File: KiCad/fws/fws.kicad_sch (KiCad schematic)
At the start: 1 part, among them U1 RP2040

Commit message: Updated schematic.
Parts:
- added U2: MIC5205-3.3YM5, Package_TO_SOT_SMD:SOT-23-5, symbol Regulator_Linear:MIC5205-3.3YM5
- added U3: W25Q128JVS, Package_SO:SOIC-8_5.23x5.23mm_P1.27mm, symbol Memory_Flash:W25Q128JVS
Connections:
- new net +3.3V: U2.5 (OUT)
- new net GND: U2.2 (GND)
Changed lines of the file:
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@@
 (kicad_sch (version 20230121) (generator eeschema)
   (paper "A4")
+  (wire (pts (xy 60.96 27.94) (xy 73.66 27.94))
+    (stroke (width 0) (type default))
+  )
+  (wire (pts (xy 53.34 38.1) (xy 53.34 40.64))
+    (stroke (width 0) (type default))
+  )
+  (wire (pts (xy 73.66 27.94) (xy 73.66 26.67))
+    (stroke (width 0) (type default))
+  )
   (symbol (lib_id "MCU_RaspberryPi:RP2040") (at 116.84 96.52 0) (unit 1)
     (in_bom yes) (on_board yes) (dnp no) (fields_autoplaced)
@@
         )
       )
+    )
+  )
+  (symbol (lib_id "Regulator_Linear:MIC5205-3.3YM5") (at 53.34 30.48 0) (unit 1)
+    (in_bom yes) (on_board yes) (dnp no) (fields_autoplaced)
+    (property "Reference" "U2" (at 53.34 21.59 0)
+      (effects (font (size 1.27 1.27)))
+    )
+    (property "Value" "MIC5205-3.3YM5" (at 53.34 24.13 0)
+      (effects (font (size 1.27 1.27)))
+    )
+    (property "Footprint" "Package_TO_SOT_SMD:SOT-23-5" (at 53.34 22.225 0)
+      (effects (font (size 1.27 1.27)) hide)
+    )
+    (property "Datasheet" "http://ww1.microchip.com/downloads/en/DeviceDoc/20005785A.pdf" (at 53.34 30.48 0)
+      (effects (font (size 1.27 1.27)) hide)
+    )
+    (pin "1")
+    (pin "2")
+    (pin "3")
+    (pin "4")
+    (pin "5")
+    (instances
+      (project "fws"
+        (path "/1464a0f5-893a-45f7-94f1-a97986ba6c99"
+          (reference "U2") (unit 1)
+        )
+      )
+    )
+  )
+  (symbol (lib_id "power:+3.3V") (at 73.66 26.67 0) (unit 1)
+    (in_bom yes) (on_board yes) (dnp no) (fields_autoplaced)
+    (property "Reference" "#PWR01" (at 73.66 30.48 0)
+      (effects (font (size 1.27 1.27)) hide)
+    )
+    (property "Value" "+3.3V" (at 73.66 21.59 0)
+      (effects (font (size 1.27 1.27)))
+    )
+    (property "Footprint" "" (at 73.66 26.67 0)
+      (effects (font (size 1.27 1.27)) hide)
+    )
+    (property "Datasheet" "" (at 73.66 26.67 0)
+      (effects (font (size 1.27 1.27)) hide)
+    )
+    (pin "1")
+    (instances
+      (project "fws"
+        (path "/1464a0f5-893a-45f7-94f1-a97986ba6c99"
+          (reference "#PWR01") (unit 1)
+        )
+      )
+    )
+  )
+  (symbol (lib_id "power:GND") (at 53.34 40.64 0) (unit 1)
+    (in_bom yes) (on_board yes) (dnp no) (fields_autoplaced)
+    (property "Reference" "#PWR02" (at 53.34 46.99 0)
+      (effects (font (size 1.27 1.27)) hide)
+    )
+    (property "Value" "GND" (at 53.34 45.72 0)
+      (effects (font (size 1.27 1.27)))
+    )
+    (property "Footprint" "" (at 53.34 40.64 0)
+      (effects (font (size 1.27 1.27)) hide)
+    )
+    (property "Datasheet" "" (at 53.34 40.64 0)
+      (effects (font (size 1.27 1.27)) hide)
+    )
+    (pin "1")
+    (instances
+      (project "fws"
+        (path "/1464a0f5-893a-45f7-94f1-a97986ba6c99"
+          (reference "#PWR02") (unit 1)
+        )
+      )
+    )
+  )
+  (symbol (lib_id "Memory_Flash:W25Q128JVS") (at 204.47 44.45 0) (unit 1)
+    (in_bom yes) (on_board yes) (dnp no) (fields_autoplaced)
+    (property "Reference" "U3" (at 213.36 43.18 0)
+      (effects (font (size 1.27 1.27)) (justify left))
+    )
+    (property "Value" "W25Q128JVS" (at 213.36 45.72 0)
+      (effects (font (size 1.27 1.27)) (justify left))
+    )
+    (property "Footprint" "Package_SO:SOIC-8_5.23x5.23mm_P1.27mm" (at 204.47 44.45 0)
+      (effects (font (size 1.27 1.27)) hide)
+    )
+    (property "Datasheet" "http://www.winbond.com/resource-files/w25q128jv_dtr%20revc%2003272018%20plus.pdf" (at 204.47 44.45 0)
+      (effects (font (size 1.27 1.27)) hide)
+    )
+    (pin "1")
+    (pin "2")
+    (pin "3")
+    (pin "4")
+    (pin "5")
+    (pin "6")
+    (pin "7")
+    (pin "8")
+    (instances
+      (project "fws"
+        (path "/1464a0f5-893a-45f7-94f1-a97986ba6c99"
+          (reference "U3") (unit 1)
+        )
+      )

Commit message: Updated schematics.
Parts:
- added J1, J2: Conn_01x03_Socket, symbol Connector:Conn_01x03_Socket
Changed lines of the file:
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@@
+    )
+  )
+  (symbol (lib_id "Connector:Conn_01x03_Socket") (at 213.36 105.41 0) (unit 1)
+    (in_bom yes) (on_board yes) (dnp no) (fields_autoplaced)
+    (property "Reference" "J1" (at 214.63 104.14 0)
+      (effects (font (size 1.27 1.27)) (justify left))
+    )
+    (property "Value" "Conn_01x03_Socket" (at 214.63 106.68 0)
+      (effects (font (size 1.27 1.27)) (justify left))
+    )
+    (property "Footprint" "" (at 213.36 105.41 0)
+      (effects (font (size 1.27 1.27)) hide)
+    )
+    (property "Datasheet" "~" (at 213.36 105.41 0)
+      (effects (font (size 1.27 1.27)) hide)
+    )
+    (pin "1")
+    (pin "2")
+    (pin "3")
+    (instances
+      (project "fws"
+        (path "/1464a0f5-893a-45f7-94f1-a97986ba6c99"
+          (reference "J1") (unit 1)
+        )
+      )
     )
   )
@@
         )
       )
+    )
+  )
+  (symbol (lib_id "Connector:Conn_01x03_Socket") (at 214.63 121.92 0) (unit 1)
+    (in_bom yes) (on_board yes) (dnp no) (fields_autoplaced)
+    (property "Reference" "J2" (at 215.9 120.65 0)
+      (effects (font (size 1.27 1.27)) (justify left))
+    )
+    (property "Value" "Conn_01x03_Socket" (at 215.9 123.19 0)
+      (effects (font (size 1.27 1.27)) (justify left))
+    )
+    (property "Footprint" "" (at 214.63 121.92 0)
+      (effects (font (size 1.27 1.27)) hide)
+    )
+    (property "Datasheet" "~" (at 214.63 121.92 0)
+      (effects (font (size 1.27 1.27)) hide)
+    )
+    (pin "1")
+    (pin "2")
+    (pin "3")
+    (instances
+      (project "fws"
+        (path "/1464a0f5-893a-45f7-94f1-a97986ba6c99"
+          (reference "J2") (unit 1)
+        )
+      )

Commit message: Various kicad project updates.
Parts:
- removed J1, J2: Conn_01x03_Socket, symbol Connector:Conn_01x03_Socket
- removed U1: RP2040, Package_DFN_QFN:QFN-56-1EP_7x7mm_P0.4mm_EP3.2x3.2mm, symbol MCU_RaspberryPi:RP2040
- removed U2: MIC5205-3.3YM5, Package_TO_SOT_SMD:SOT-23-5, symbol Regulator_Linear:MIC5205-3.3YM5
- removed U3: W25Q128JVS, Package_SO:SOIC-8_5.23x5.23mm_P1.27mm, symbol Memory_Flash:W25Q128JVS
- added J1, J2: SM03B-SRSS-TB_LF__SN_, fws:SM03B-SRSS-TB_LF__SN_, symbol FWS:SM03B-SRSS-TB_LF__SN_
- added U1: MIC5205-3.3YM5, Package_TO_SOT_SMD:SOT-23-5, symbol FWS:MIC5205-3.3YM5
- added U2: RP2040, Package_DFN_QFN:QFN-56-1EP_7x7mm_P0.4mm_EP3.2x3.2mm, symbol FWS:RP2040
- added U3: W25Q128JVS, Package_SO:SOIC-8_5.23x5.23mm_P1.27mm, symbol FWS:W25Q128JVS
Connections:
- new net: U2.1 (IOVDD), U2.10 (IOVDD), U2.22 (IOVDD), U2.33 (IOVDD), U2.42 (IOVDD), U2.49 (IOVDD)
- new net: U2.23 (DVDD), U2.50 (DVDD)
- new net: J2.S1 (SHIELD), J2.S2 (SHIELD)
- new net: J1.S1 (SHIELD), J1.S2 (SHIELD)

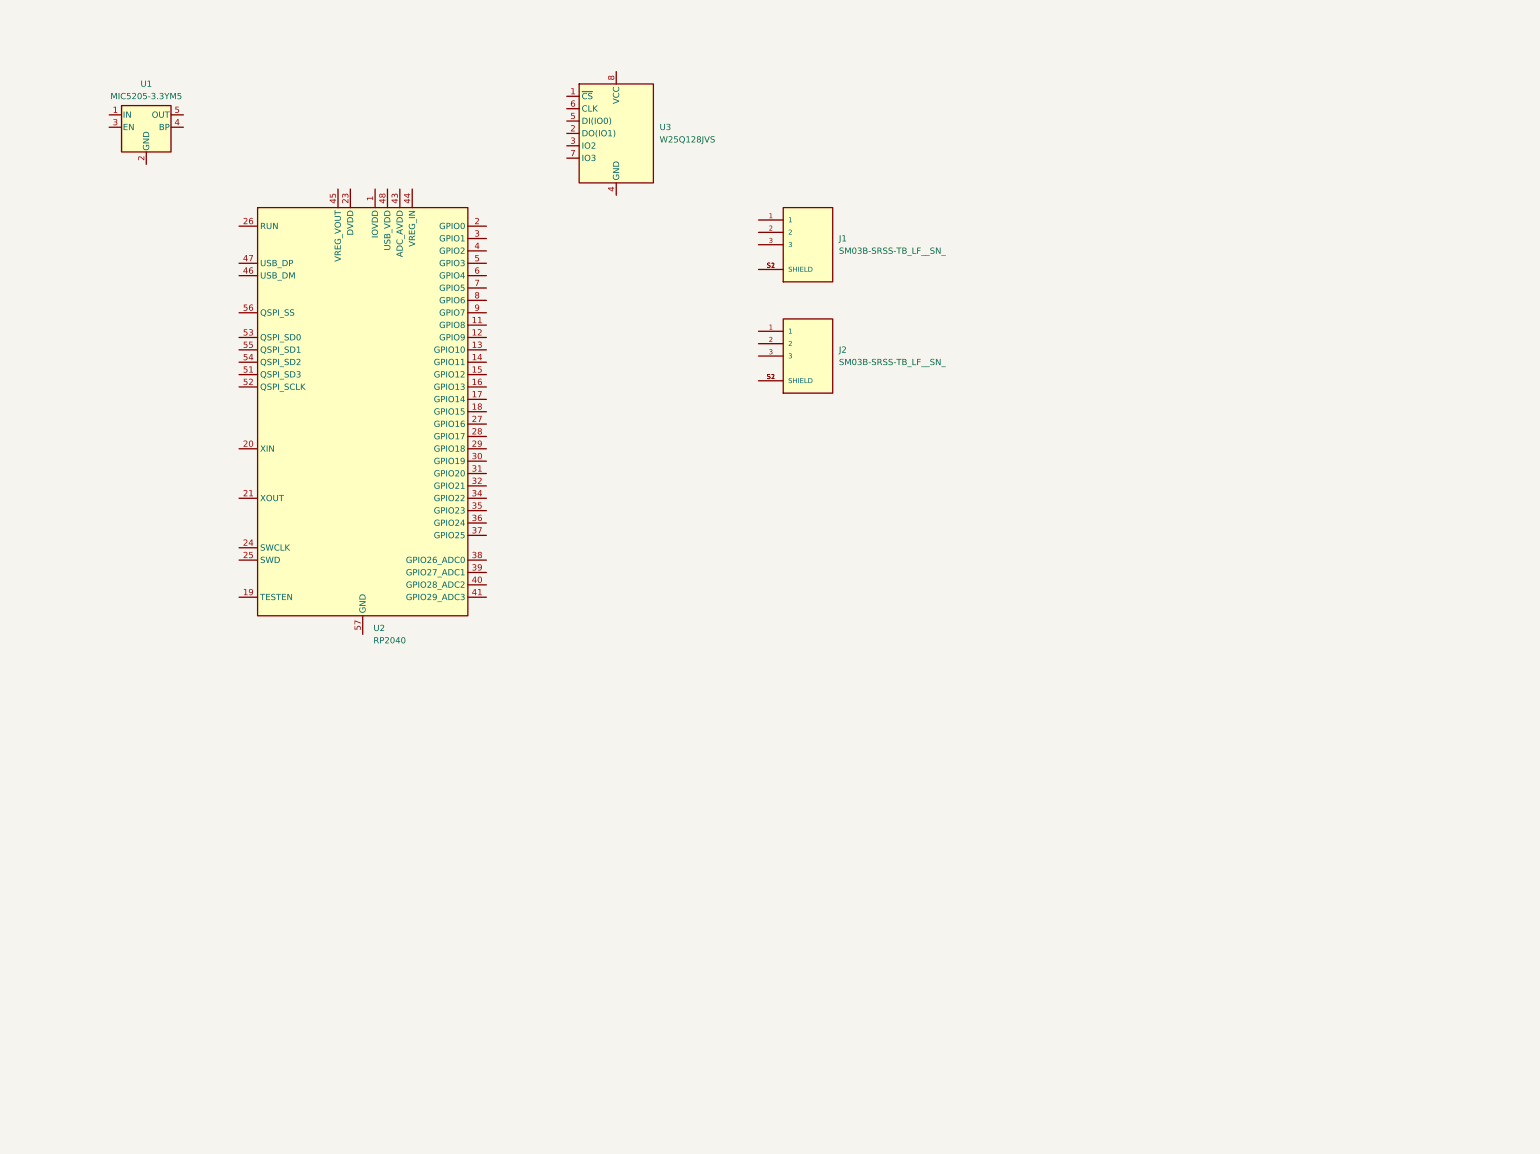
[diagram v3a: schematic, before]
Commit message: Added power and usbc.
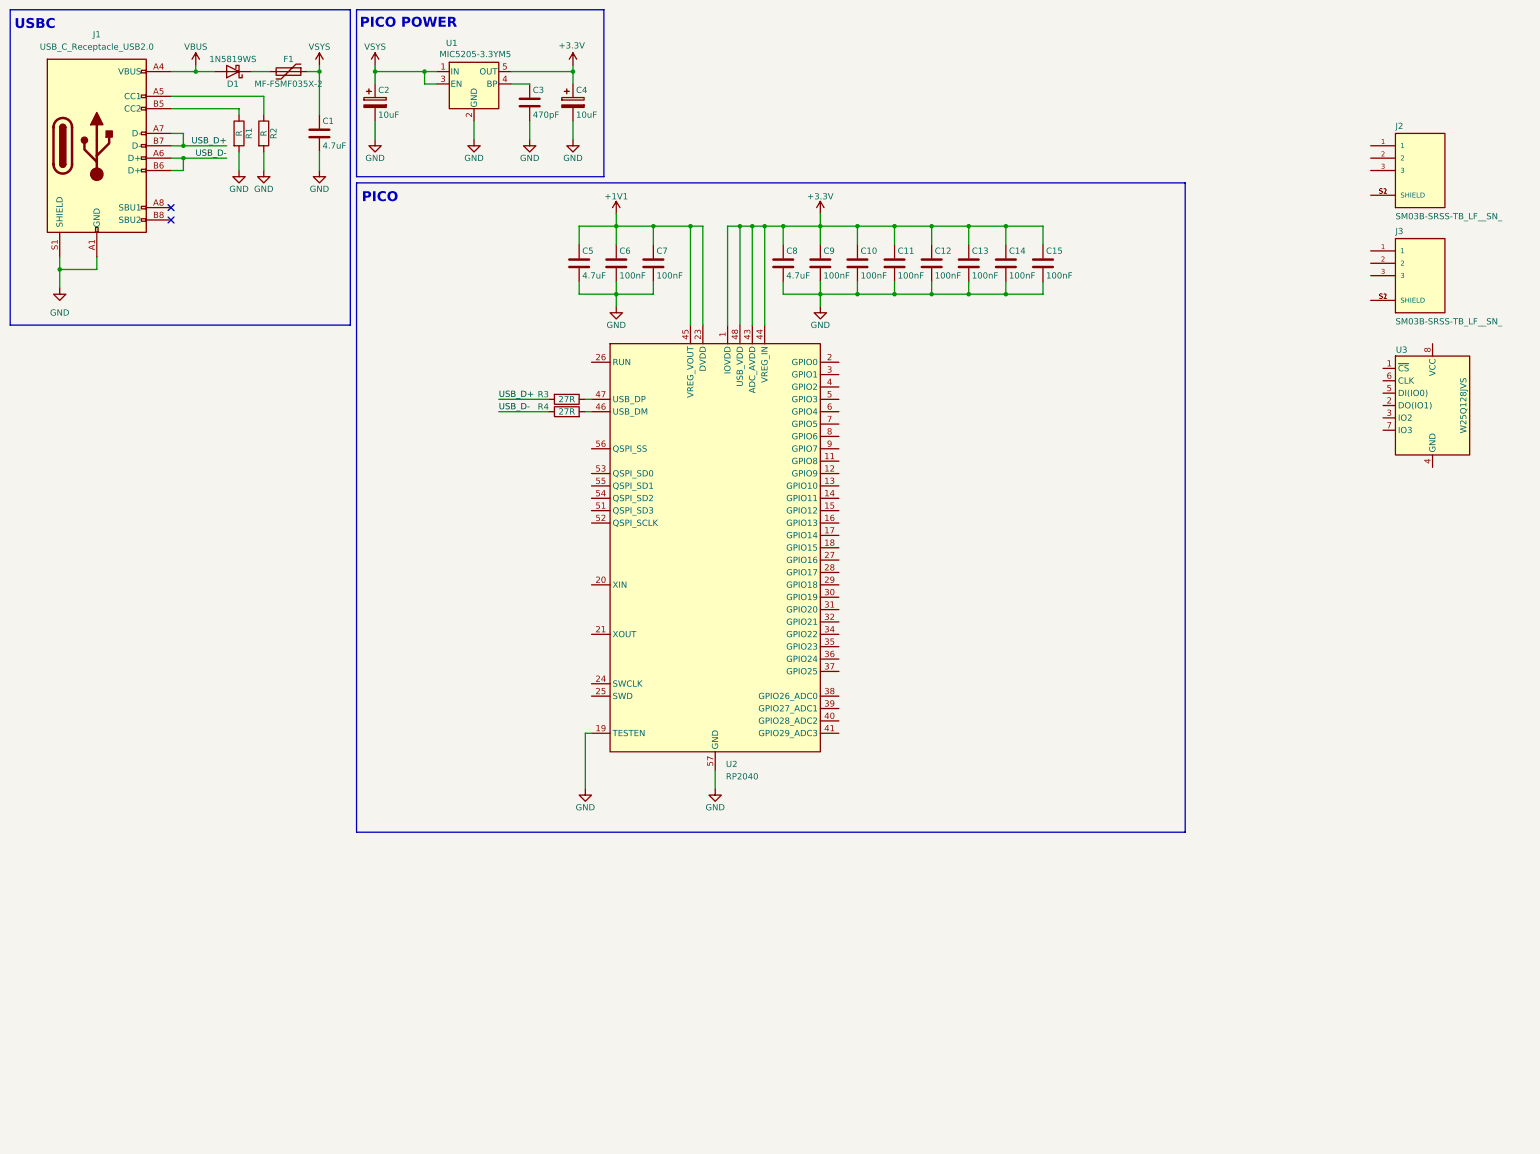
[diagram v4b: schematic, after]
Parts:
- removed J1: SM03B-SRSS-TB_LF__SN_, fws:SM03B-SRSS-TB_LF__SN_, symbol FWS:SM03B-SRSS-TB_LF__SN_
- added C1, C5, C8: 4.7uF, symbol FWS:C
- added C10, C11, C12, C13, C14, C15, C6, C7, C9: 100nF, symbol FWS:C
- added C2, C4: 10uF, symbol FWS:C_Polarized
- added C3: 470pF, symbol FWS:C
- added D1: 1N5819WS, Diode_SMD:D_SOD-323, symbol FWS:1N5819WS
- added F1: MF-FSMF035X-2, symbol FWS:Polyfuse
- added J1: USB_C_Receptacle_USB2.0, symbol FWS:USB_C_Receptacle_USB2.0
- added J3: SM03B-SRSS-TB_LF__SN_, fws:SM03B-SRSS-TB_LF__SN_, symbol FWS:SM03B-SRSS-TB_LF__SN_
- added R1, R2: R, symbol FWS:R
- added R3, R4: 27R, symbol FWS:R
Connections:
- net +3.3V: now reaches U2.1 (IOVDD), U2.10 (IOVDD), U2.22 (IOVDD), U2.33 (IOVDD), U2.42 (IOVDD), U2.49 (IOVDD)
- net +3.3V: now also U1.5 (OUT), U2.43 (ADC_AVDD), U2.44 (VREG_IN), U2.48 (USB_VDD), C10.1, C11.1, C12.1, C13.1, C14.1, C15.1, C4.1, C8.1, C9.1
- net GND: now reaches U2.19 (TESTEN)
- net GND: now also U1.2 (GND), U2.57 (GND), C1.2, C10.2, C11.2, C12.2, C13.2, C14.2, C15.2, C2.2, C3.2, C4.2, C5.2, C6.2, C7.2, C8.2, C9.2, J1.A1 (GND), J1.A12 (GND), J1.B1 (GND), J1.B12 (GND), J1.S1 (SHIELD), R1.2, R2.2
- net +1V1: now reaches U2.23 (DVDD), U2.50 (DVDD)
- net +1V1: now also U2.45 (VREG_VOUT), C5.1, C6.1, C7.1
- net at U2.46 (USB_DM): now also R4.2
- net at U2.47 (USB_DP): now also R3.1
- net VSYS: now reaches U1.1 (IN)
- net VSYS: now also U1.3 (EN), C1.1, C2.1, F1.1
- net at U1.4 (BP): now also C3.1
- new net: J1.A5 (CC1), R2.1
- new net: J1.B5 (CC2), R1.1
- new net: J3.S1 (SHIELD), J3.S2 (SHIELD)
- new net: D1.1 (K), F1.2
- new net USB_D+: J1.A7 (D-), J1.B7 (D-), R3.2
- new net USB_D-: J1.A6 (D+), J1.B6 (D+), R4.1
- new net VBUS: D1.2 (A), J1.A4 (VBUS), J1.A9 (VBUS), J1.B4 (VBUS), J1.B9 (VBUS)
- no-connect marks 0 -> 2
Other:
- note added: "PICO"
- note added: "PICO POWER"
- note added: "USBC"
- moved on the sheet: U2

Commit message: Added flash.
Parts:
- added C?: 100nF, symbol FWS:C
- added R?: 10K, symbol FWS:R
- added R?: 1K, symbol FWS:R
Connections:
- net +3.3V: now also U3.8 (VCC), C?.1, R?.1
- net GND: now also U3.4 (GND), C?.2
- net QSPI_SD3: now reaches U2.51 (QSPI_SD3)
- net QSPI_SD3: now also U3.7 (IO3)
- net QSPI_SCLK: now reaches U2.52 (QSPI_SCLK)
- net QSPI_SCLK: now also U3.6 (CLK)
- net QSPI_SD0: now reaches U2.53 (QSPI_SD0)
- net QSPI_SD0: now also U3.5 (DI(IO0))
- net QSPI_SD2: now reaches U2.54 (QSPI_SD2)
- net QSPI_SD2: now also U3.3 (IO2)
- net QSPI_SD1: now reaches U2.55 (QSPI_SD1)
- net QSPI_SD1: now also U3.2 (DO(IO1))
- net QSPI_SS: now reaches U2.56 (QSPI_SS)
- net QSPI_SS: now also U3.1 (~{CS}), R?.2, R?.2
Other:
- note added: "FLASH"
- moved on the sheet: U3

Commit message: Added clock.
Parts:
- added C? (x2): 27pF, symbol FWS:C
- added R?: 10K, symbol FWS:R
- added Y?: 12MHz, symbol FWS:Crystal_GND24
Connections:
- net +3.3V: now also R?.1
- net GND: now also C?.1, C?.1, Y?.2, Y?.4
- net at U2.20 (XIN): now also C?.2, Y?.3
- net at U2.21 (XOUT): now also C?.2, Y?.1
- net SWCLK: now reaches U2.24 (SWCLK)
- net SWD: now reaches U2.25 (SWD)
- net at U2.26 (RUN): now also R?.2
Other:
- moved on the sheet: J2, J3

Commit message: Updated fws schematics.
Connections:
- net GND: now also J2.2, J2.S1 (SHIELD), J2.S2 (SHIELD)
- net SWCLK: now also J2.1
- net SWD: now also J2.3
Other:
- note added: "SWD"
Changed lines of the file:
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@@
   (junction (at 152.4 57.15) (diameter 0) (color 0 0 0 0)
+  )
+  (junction (at 48.26 166.37) (diameter 0) (color 0 0 0 0)
   )
   (junction (at 87.63 25.4) (diameter 0) (color 0 0 0 0)
@@
     (stroke (width 0) (type default))
   )
+  (wire (pts (xy 48.26 158.75) (xy 48.26 166.37))
+    (stroke (width 0) (type default))
+  )
   (wire (pts (xy 30.48 66.04) (xy 22.86 66.04))
     (stroke (width 0) (type default))
@@
     (stroke (width 0) (type default))
   )
+  (wire (pts (xy 41.91 161.29) (xy 50.8 161.29))
+    (stroke (width 0) (type default))
+  )
   (wire (pts (xy 120.65 85.09) (xy 123.19 85.09))
     (stroke (width 0) (type default))
@@
     (stroke (width 0) (type default))
   )
+  (wire (pts (xy 48.26 166.37) (xy 48.26 168.91))
+    (stroke (width 0) (type default))
+  )
   (wire (pts (xy 119.38 144.78) (xy 124.46 144.78))
     (stroke (width 0) (type default))
@@
     (stroke (width 0) (type default))
   )
+  (wire (pts (xy 41.91 156.21) (xy 50.8 156.21))
+    (stroke (width 0) (type default))
+  )
   (wire (pts (xy 50.8 100.33) (xy 50.8 102.87))
     (stroke (width 0) (type default))
@@
     (stroke (width 0) (type default))
   )
+  (wire (pts (xy 48.26 166.37) (xy 50.8 166.37))
+    (stroke (width 0) (type default))
+  )
   (wire (pts (xy 137.16 57.15) (xy 137.16 60.96))
     (stroke (width 0) (type default))
@@
   )
   (wire (pts (xy 217.17 57.15) (xy 224.79 57.15))
+    (stroke (width 0) (type default))
+  )
+  (wire (pts (xy 50.8 158.75) (xy 48.26 158.75))
     (stroke (width 0) (type default))
   )
@@
   (text "USBC" (exclude_from_sim no)
  (at 17.78 15.748 0)
+    (effects (font (size 2.032 2.032) (thickness 0.4064) bold))
+  )
+  (text "SWD" (exclude_from_sim no)
+ (at 18.288 150.114 0)
     (effects (font (size 2.032 2.032) (thickness 0.4064) bold))
   )
@@
         )
       )
+    )
+  )
+  (symbol (lib_id "FWS:GND") (at 48.26 168.91 0) (unit 1)
+    (exclude_from_sim no) (in_bom yes) (on_board yes) (dnp no)
+    (property "Reference" "#PWR025" (at 48.26 175.26 0)
+      (effects (font (size 1.27 1.27)) hide)
+    )
+    (property "Value" "GND" (at 48.26 172.72 0)
+      (effects (font (size 1.27 1.27)))
+    )
+    (property "Footprint" "" (at 48.26 168.91 0)
+      (effects (font (size 1.27 1.27)) hide)
+    )
+    (property "Datasheet" "" (at 48.26 168.91 0)
+      (effects (font (size 1.27 1.27)) hide)
+    )
+    (property "Description" "Power symbol creates a global label with name \"GND\" , ground" (at 48.26 168.91 0)
+      (effects (font (size 1.27 1.27)) hide)
+    )
+    (pin "1")
+    (instances
+      (project "fws"
+        (path "/1464a0f5-893a-45f7-94f1-a97986ba6c99"
+          (reference "#PWR025") (unit 1)
+        )
+      )

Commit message: Updated schematics.
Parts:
- added S?: ~, FWS:s13131-1536, symbol FWS:S13131
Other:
- note added: "s13131"
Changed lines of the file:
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@@
+    (fill (type none))
+  )
+  (rectangle (start 135.89 12.7) (end 205.74 46.99)
+    (stroke (width 0) (type default))
     (fill (type none))
   )
@@
     (stroke (width 0) (type default))
     (fill (type none))
+  )
+  (text "s13131" (exclude_from_sim no)
+ (at 142.494 15.494 0)
+    (effects (font (size 2.032 2.032) (thickness 0.4064) bold))
   )
   (text "FLASH" (exclude_from_sim no)
@@
         )
       )
+    )
+  )
+  (symbol (lib_id "FWS:S13131") (at 170.18 29.21 0) (unit 1)
+    (exclude_from_sim no) (in_bom yes) (on_board yes) (dnp no)
+    (property "Reference" "S?" (at 167.386 21.59 0)
+      (effects (font (size 1.27 1.27)))
+    )
+    (property "Value" "~" (at 170.18 31.75 0)
+      (effects (font (size 1.27 1.27)))
+    )
+    (property "Footprint" "FWS:s13131-1536" (at 170.18 31.75 0)
+      (effects (font (size 1.27 1.27)) hide)
+    )
+    (property "Datasheet" "" (at 170.18 31.75 0)
+      (effects (font (size 1.27 1.27)) hide)
+    )
+    (property "Description" "" (at 170.18 31.75 0)
+      (effects (font (size 1.27 1.27)) hide)
+    )
+    (pin "4")
+    (pin "5")
+    (pin "2")
+    (pin "6")
+    (pin "7")
+    (pin "8")
+    (pin "3")
+    (pin "1")
+    (instances
+      (project "fws"
+        (path "/1464a0f5-893a-45f7-94f1-a97986ba6c99"
+          (reference "S?") (unit 1)
+        )
+      )
